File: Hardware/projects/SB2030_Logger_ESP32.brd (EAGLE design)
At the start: 96.8 x 48.4 mm, 91 parts, among them IC1 MPU6050, T2 S8050, T3 S8050, T4 S8050, U1 ESP32-WROOM-32E, U2 TLA1051T/3, U3 AMS1117-5.0, U4 AMS1117-3.3, U5 SN65C1168PWR, X1 1751280

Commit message: Debugging fixes for NEMO-30 and WIBL support - Added builds for NEMO-30 separate from prototype loggers and WIBL - Added pass-back for value read from ADC for power monitoring - Pushed CAN traffic to GPIO16/17 to avoid interference with SD/MMC interface.
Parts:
- U2: value TLA1051T/3 -> TJA1051T/3
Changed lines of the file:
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@@
 <drawing>
 <settings>
-<setting alwaysvectorfont="yes"/>
+<setting alwaysvectorfont="no"/>
 <setting verticaltext="up"/>
 </settings>
@@
 <attribute name="VALUE" x="28.829" y="10.033" size="1.27" layer="27"/>
 </element>
-<element name="U2" library="sb2030_logger" package="SOIC8" value="TLA1051T/3" x="90.7669" y="33.147" smashed="yes" rot="R270">
+<element name="U2" library="sb2030_logger" package="SOIC8" value="TJA1051T/3" x="90.7669" y="33.147" smashed="yes" rot="R270">
 <attribute name="NAME" x="86.9569" y="29.8831" size="0.762" layer="25"/>
 </element>

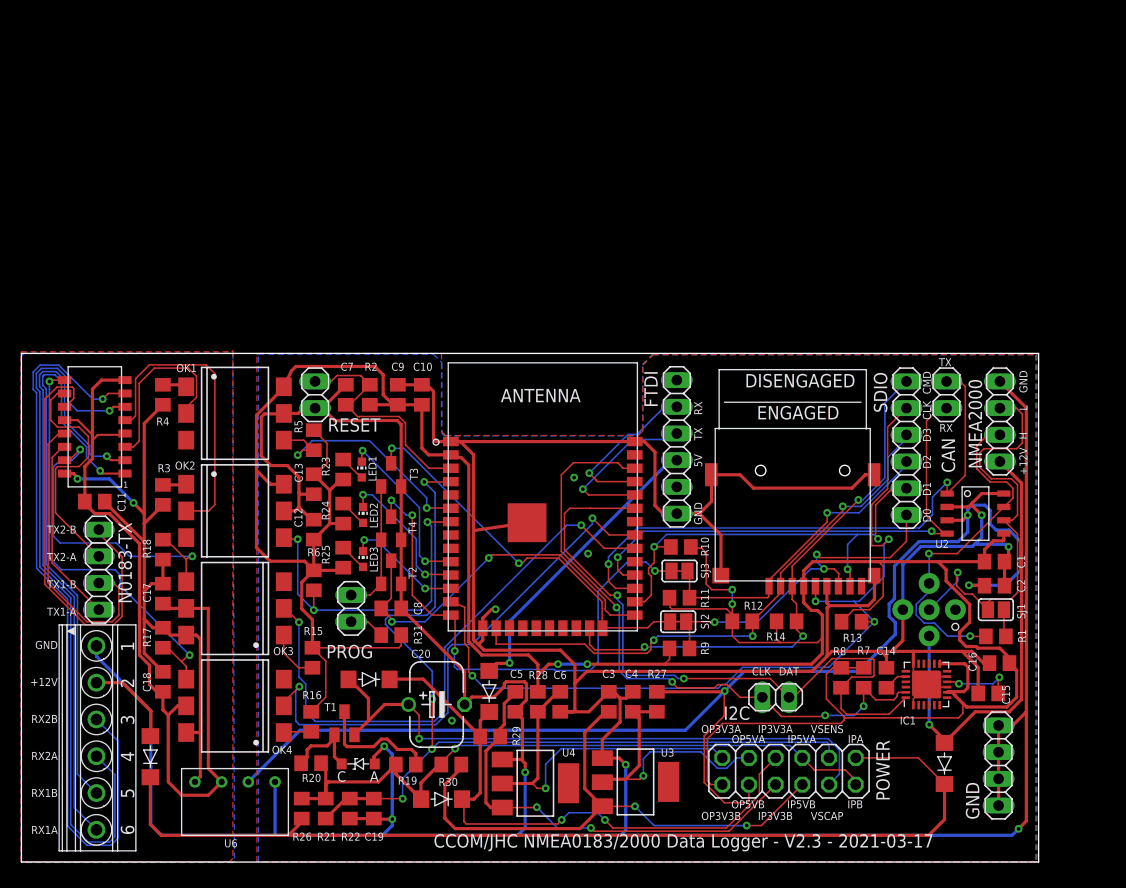
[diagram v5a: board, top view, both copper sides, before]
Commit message: Updates to logger schematic and board layout.
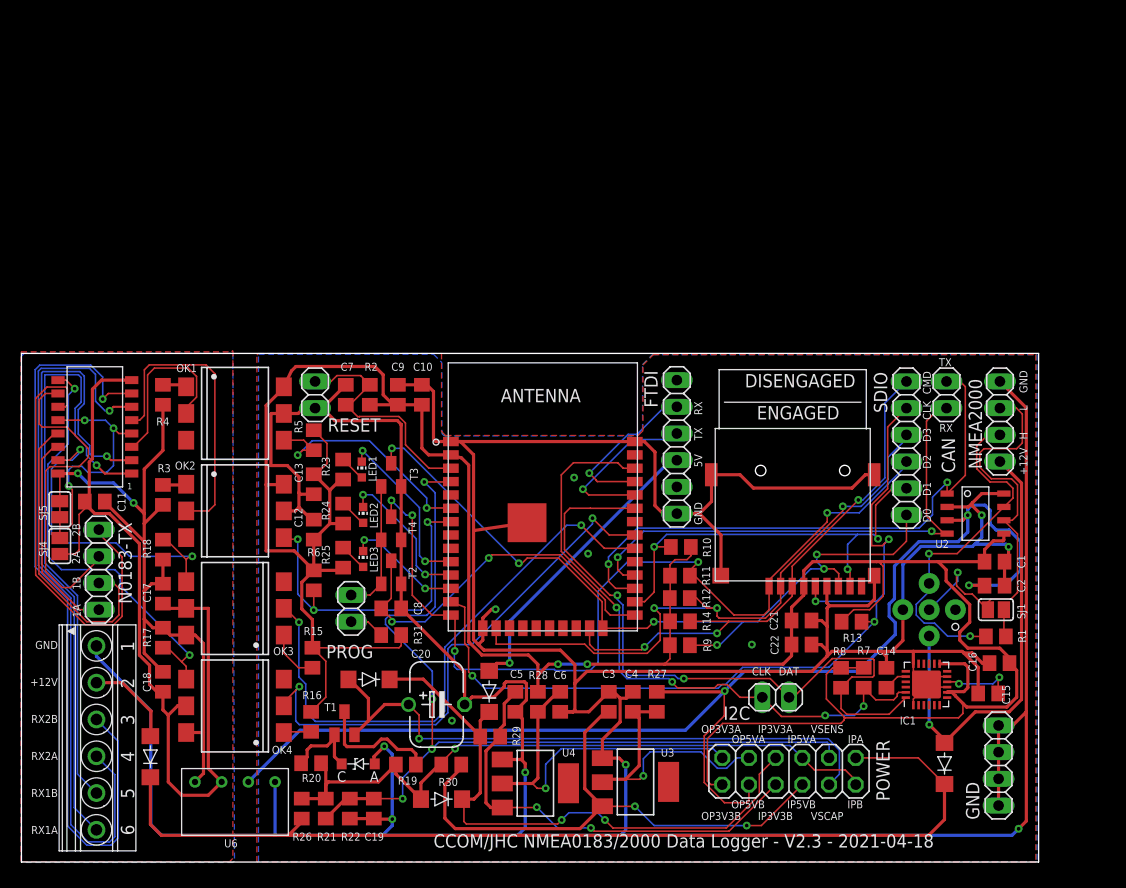
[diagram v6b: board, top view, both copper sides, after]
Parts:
- removed SJ2, SJ3: (no value), jumper:SJ
- added C21: 10u, rcl:C0805
- added C22: 0.1u, rcl:C0805
- added SJ4, SJ5: (no value), jumper:SJ
- U5: value SN65C1168PWR -> SN65C1168NSR
- moved R14 10.1 mm to (62.7, 22.9)
- moved R12 6.34 mm to (62.6, 25.1)
- moved R11 2.10 mm to (62.6, 27.2)
- moved R9 0.31 mm to (62.6, 20.6)
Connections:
- net +3V3: now also C21.1, C22.1
- net GND: now also C21.2, C22.2
- net GNDI: now also SJ4.1, U5.8; no longer U5.1DE, U5.2DE, U5.GND
- net N$10: no longer SJ3.1, SJ3.2
- net N$13: now also U5.3; no longer U5.1R
- net N$14: now also U5.5; no longer U5.2R
- net N$17: now also U5.2; no longer U5.1A
- net N$18: now also U5.1; no longer U5.1B
- net N$19: now also U5.6; no longer U5.2A
- net N$20: now also U5.7; no longer U5.2B
- net N$21: now also SJ4.2, SJ5.1, SJ5.2, U5.12, U5.16, U5.4; no longer U5.VCC
- net N$22: no longer SJ2.1, SJ2.2
- net N$27: now also U5.14; no longer U5.1Y
- net N$28: now also U5.13; no longer U5.1Z
- net N$29: now also U5.10; no longer U5.2Y
- net N$30: now also U5.11; no longer U5.2Z
- net N$33: now also U5.15; no longer U5.1D
- net N$34: now also U5.9; no longer U5.2D
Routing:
- net N$21: track 69.6 -> 99.5 mm, vias 2 -> 5
- net +3V3: track 301.6 -> 276.0 mm, vias 4 -> 2
- net N$29: track 23.3 -> 32.1 mm
- net N$24: track 53.6 -> 59.7 mm
- net N$22: track 72.9 -> 76.0 mm, vias 5 -> 6
- net N$10: track 82.5 -> 85.1 mm
- net N$17: track 60.0 -> 62.3 mm
- net N$18: track 56.4 -> 58.5 mm
- net GND: track 507.7 -> 509.5 mm, vias 11 -> 12
- net N$20: track 73.1 -> 74.8 mm
- net N$27: track 17.9 -> 19.7 mm
- net N$30: track 41.5 -> 42.5 mm
- net GNDI: track 81.9 -> 82.8 mm
- net N$34: track 41.2 -> 42.1 mm
- net N$33: track 31.7 -> 32.5 mm
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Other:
- board text added: "(c) 2021 Center for Coastal and Ocean Mapping University of New Hampshire 2021-04-18 V2.3"
- board text added: "1A"
- board text added: "1B"
- board text added: "2A"
- board text added: "2B"
- board text added: "CCOM/JHC NMEA0183/2000 Data Logger - V2.3 - 2021-04-18"
- board text removed: "(c) 2021 Center for Coastal and Ocean Mapping University of New Hampshire 2021-03-17 V2.3"
- board text removed: "CCOM/JHC NMEA0183/2000 Data Logger - V2.3 - 2021-03-17"
- board text removed: "TX1-A"
- board text removed: "TX1-B"
- board text removed: "TX2-A"
- board text removed: "TX2-B"

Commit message: Updates to design for WIBL, board and schematic, to match new SMPS integration, and other small fixes for layout of power input, and super-capacitor charging circuit.
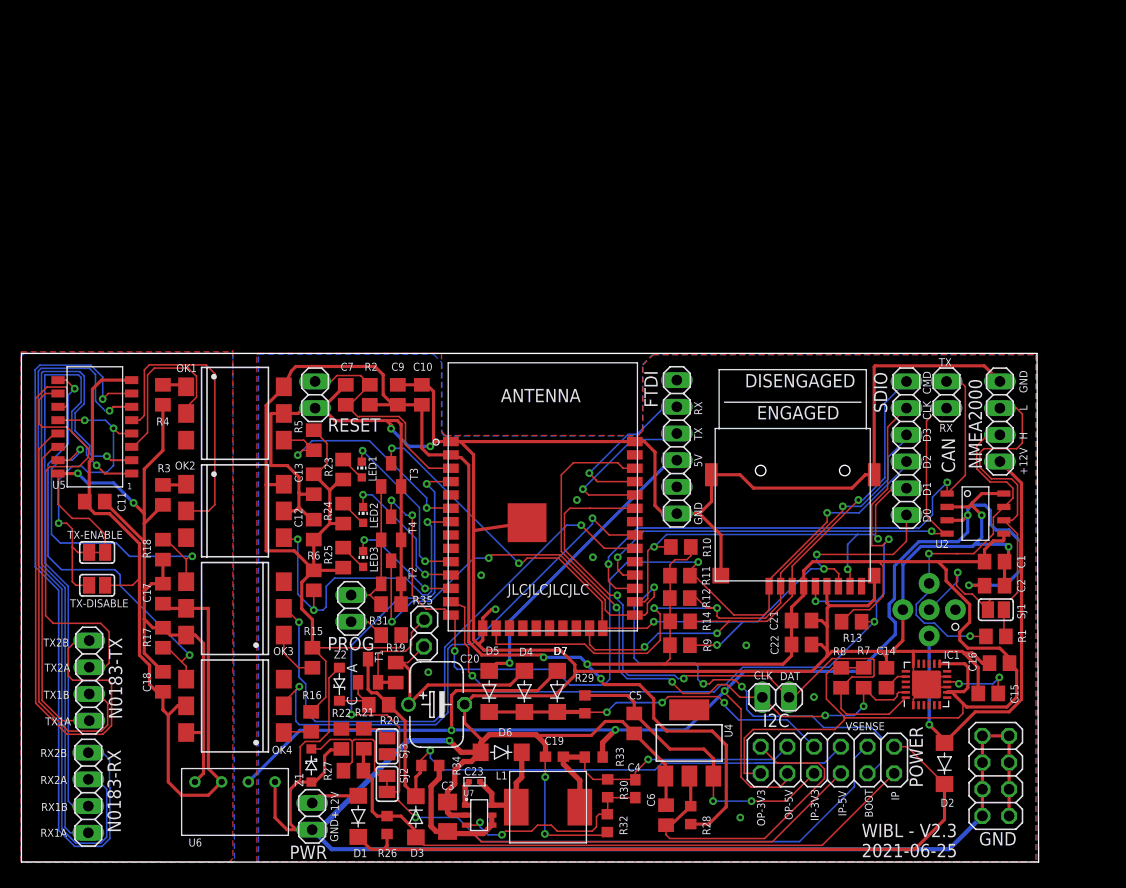
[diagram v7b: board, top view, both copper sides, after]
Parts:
- removed C8: 0.1u, rcl:C0805
- removed SJ4, SJ5: (no value), jumper:SJ
- removed U3: AMS1117-5.0, burr-brown:SOT223
- removed X1: 1751280, con-phoenix-350:1751280
- added C23: 100nF, sb2030_logger:C0402
- added D6, D7: SS14, sb2030_logger:DO-214AC
- added JP1, JP3: (no value), pinhead:1X01
- added L1: 15uH, sb2030_logger:MWSA0603S
- added N0183-RX: (no value), pinhead:1X04
- added PWR: (no value), pinhead:1X02
- added R32: 23.7k, rcl:R0603
- added R33, R34: 0R1, rcl:R0603
- added R35: 47k, rcl:R0805
- added SJ2, SJ3, TX-DISABLE, TX-ENABLE: (no value), jumper:SJ
- added U7: (no value), sb2030_logger:SOT-23-6L
- added Z2: DZL4734, sb2030_logger:SOD-123FL
- C19: value 0.1u -> 22uF; device rcl:C0805 -> rcl:C0603
- C3: value 10u -> 10uF; device rcl:C0805 -> rcl:C1206
- C4: value 10u -> 33pF; device rcl:C0805 -> rcl:C0603
- C7: value 0.1u -> 1uF
- GND: device pinhead:1X04 -> pinhead:2X04
- R26, R28, R29: value 1R -> 0R1; device rcl:R0805 -> rcl:R0603
- R27: value 1R -> 1k5
- R30: value 1R -> 127k; device rcl:R0805 -> rcl:R0603
- Z1: value DZL4734 -> BZT52C3V0; device sb2030_logger:SOD-123FL -> sb2030_logger:SOD123
- moved R27 29.6 mm to (31.6, 8.69), turned to 0 degrees
- moved D1 20.6 mm to (32.0, 4.34)
- moved C3 18.8 mm to (40.5, 4.31)
- moved R28 18.1 mm to (63.7, 4.46), turned to 90 degrees
- moved C19 17.9 mm to (50.7, 10.0), turned to 0 degrees
- moved U4 15.1 mm to (63.5, 11.3), turned to 0 degrees
- moved R30 15.1 mm to (55.8, 7.01), turned to 90 degrees
- moved D4 14.8 mm to (47.9, 16.2), turned to 90 degrees
- moved C6 14.8 mm to (61.3, 4.46), turned to 90 degrees
- moved C5 11.5 mm to (58.3, 13.2)
- moved N0183-TX 10.6 mm to (6.45, 17.3)
- moved R29 9.51 mm to (53.6, 15.0), turned to 270 degrees
- moved R19 8.80 mm to (35.6, 18.0), turned to 270 degrees
- moved R20 8.51 mm to (34.0, 15.0)
- moved C4 8.27 mm to (58.4, 6.97)
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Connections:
- net IP_CUR_3V3_B renamed IP_CUR_3V3_L
- net IP_CUR_A renamed IP_CUR_H
- net OP_CUR_3V3_A renamed OP_CUR_3V3_H
- removed net IP_CUR_3V3_A: D3.K, D4.K, D5.K, POWER.7, R29.2
- removed net IP_CUR_5V_B: C3.1, POWER.6, R30.1, U3.3
- removed net IP_CUR_B: D3.A, POWER.2, POWER.5, R19.2, R20.2, R21.2, R26.1, R30.2
- removed net N$12: C8.1, T2.3, U1.25
- removed net OP_CUR_5V_A: C4.1, POWER.9, R27.2, U3.2
- new net BOOT: POWER.4, T2.3, U1.25
- new net IP_CUR_3V3_H: D4.K, D5.K, D7.K, POWER.7, R29.2
- new net IP_CUR_5V_H: D3.K, POWER.5, R20.2, R34.2, T1.C
- new net IP_CUR_5V_L: C3.1, POWER.6, R34.1, U7.4, U7.5
- new net IP_CUR_L: D3.A, POWER.2, R21.2, R26.1, R27.2
- new net N$45: C23.P$2, D6.K, L1.P$1, U7.6
- new net N$46: R21.1, R22.2, SJ3.2
- new net N$48: C4.1, R30.1, R32.2, U7.3
- new net OP_CUR_5V_H: C19.2, C4.2, L1.P$2, POWER.9, R30.2, R33.2
- new net SCAPDRV: JP1.1, R19.2, T1.E
- net +12V: now also PWR.2; no longer X1.2
- net +5V: now also D7.A, R33.1; no longer R27.1
- net GND: now also C19.1, D6.A, GND.5, GND.6, GND.7, GND.8, PWR.1, R32.1, R35.1, U7.2, Z1.1, Z2.A; no longer C19.2, C4.2, C8.2, U3.1, X1.1, Z1.A
- net GNDI: now also TX-DISABLE.1; no longer SJ4.1
- net N$17: now also N0183-RX.4; no longer X1.6
- net N$18: now also N0183-RX.3; no longer X1.5
- net N$19: now also N0183-RX.2; no longer X1.4
- net N$20: now also N0183-RX.1; no longer X1.3
- net N$21: now also TX-DISABLE.2, TX-ENABLE.1, TX-ENABLE.2; no longer SJ4.2, SJ5.1, SJ5.2
- net N$37: now also R35.2
- net N$41: now also Z2.K; no longer Z1.K
- net N$42: now also C23.P$1, U7.1; no longer R19.1, T1.C
- net SCAP: now also JP3.1, R19.1; no longer POWER.4, T1.E
- net VSENSE: now also R27.1, SJ2.1, SJ2.2, SJ3.1, Z1.2; no longer C19.1, R21.1, R22.2
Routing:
- net BOOT: track 0.00 -> 78.8 mm, vias 0 -> 5
- net IP_CUR_B: track 65.4 -> 0.00 mm, vias 1 -> 0
- net IP_CUR_5V_H: track 0.00 -> 61.3 mm, vias 0 -> 1
- net IP_CUR_L: track 0.00 -> 60.5 mm
- net IP_CUR_3V3_A: track 57.8 -> 0.00 mm, vias 2 -> 0
- net IP_CUR_5V_B: track 54.2 -> 0.00 mm, vias 2 -> 0
- net IP_CUR_5V_L: track 0.00 -> 51.4 mm
- net SCAP: track 58.9 -> 20.4 mm, vias 1 -> 0
- net N$12: track 35.3 -> 0.00 mm, vias 2 -> 0
- net IP_CUR_3V3_H: track 0.00 -> 33.8 mm, vias 0 -> 3
- net OP_CUR_5V_H: track 0.00 -> 30.2 mm, vias 0 -> 1
- net IP_CUR_H: track 96.0 -> 68.7 mm
- net OP_CUR_5V_A: track 26.6 -> 0.00 mm, vias 1 -> 0
- net VSENSE: track 87.7 -> 111.2 mm, vias 4 -> 3
- net N$48: track 0.00 -> 20.4 mm, vias 0 -> 2
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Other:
- outline, holes or cut-outs redrawn
- board text added: "(c) 2021 Center for Coastal and Ocean Mapping University of New Hampshire 2021-06-25 V2.3"
- board text added: "BOOT"
- board text added: "D4"
- board text added: "D5"
- board text added: "D6"
- board text added: "D7"
- board text added: "IP"
- board text added: "IP-3V3"
- board text added: "IP-5V"
- board text added: "JLCJLCJLCJLC"
- board text added: "OP-3V3"
- board text added: "OP-5V"
- board text added: "TX1A"
- board text added: "TX1B"
- board text added: "TX2A"
- board text added: "TX2B"
- board text added: "U5"
- board text added: "VSENSE"
- board text added: "WIBL - V2.3 2021-06-25"
- board text added: "Z2"
- board text removed: "(c) 2021 Center for Coastal and Ocean Mapping University of New Hampshire 2021-04-18 V2.3"
- board text removed: "1A"
- board text removed: "1B"
- board text removed: "2A"
- board text removed: "2B"
- board text removed: "CCOM/JHC NMEA0183/2000 Data Logger - V2.3 - 2021-04-18"
- board text removed: "IP3V3A"
- board text removed: "IP3V3B"
- board text removed: "IP5VA"
- board text removed: "IP5VB"
- board text removed: "IPA"
- board text removed: "IPB"
- board text removed: "OP3V3A"
- board text removed: "OP3V3B"
- board text removed: "OP5VA"
- board text removed: "OP5VB"
- board text removed: "VSCAP"
- board text removed: "VSENS"

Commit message: Please enter the commit message for your changes. Lines starting
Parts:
- removed C14: 2n2, rcl:C0805
- removed C15: 0.1u, rcl:C0805
- removed C16: 10n, rcl:C0805
- removed IC1: MPU6050, invensense:QFN50P400X400X95-25T265X275N
- added C8: 0.1u, rcl:C0805
- added R36: 10k, rcl:R0805
- added U3: LSM6DS3TR-C, LSM6DS3TR-C:LGA-14-2.5X3MM
- moved R7 9.94 mm to (90.1, 17.2)
- moved I2C 2.22 mm to (74.0, 15.4)
- moved R8 1.96 mm to (79.9, 17.3)
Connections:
- removed net N$23: C14.1, IC1.20
- removed net N$5: I2C.2, IC1.23, R7.1, U1.36
- removed net N$8: I2C.1, IC1.24, R8.1, U1.33
- removed net N$9: C15.1, IC1.10
- new net INT1: R8.1, U1.5, U3.4
- new net SCL: I2C.1, R7.1, U1.33, U3.14
- new net SDA: I2C.2, R36.1, U1.36, U3.13
- net +3V3: now also C8.1, R36.2, U3.12, U3.2, U3.3, U3.5, U3.8; no longer C16.1, IC1.13, IC1.8
- net GND: now also C8.2, U3.1, U3.6, U3.7; no longer C14.2, C15.2, C16.2, IC1.1, IC1.11, IC1.18, IC1.25, IC1.9
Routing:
- net SDA: track 0.00 -> 76.2 mm, vias 0 -> 6
- net SCL: track 0.00 -> 65.4 mm, vias 0 -> 5
- net N$8: track 65.4 -> 0.00 mm, vias 2 -> 0
- net N$5: track 61.5 -> 0.00 mm, vias 4 -> 0
- net INT1: track 0.00 -> 59.8 mm, vias 0 -> 9
- net +3V3: track 296.3 -> 286.6 mm
- net GND: track 498.1 -> 488.6 mm, vias 15 -> 10
- net N$9: track 6.87 -> 0.00 mm, vias 2 -> 0
- net N$23: track 2.28 -> 0.00 mm
- net N$25: track 83.1 -> 84.5 mm
- net N$26: track 52.0 -> 51.4 mm
- net BOOT: track 78.8 -> 78.3 mm
- net N$24: track 59.7 -> 59.2 mm
